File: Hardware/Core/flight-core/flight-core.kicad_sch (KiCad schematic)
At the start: 11 parts, among them J1 CONN_02x03_RA, J101 Conn_01x02, J106 Conn_01x02, J107 Conn_01x02, J2 CONN_02x03_RA, J3 CONN_02x03_RA, J4 CONN_02x03_RA, U2 DC DC CONVERTER 12V 240W

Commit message: adding logical gate structure without RC components in bus arbitration logic sch file
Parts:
- removed R2: R_100K, footprints:R_0805_OEM, symbol formula:R_100K
- added D1: LED_0805_Amber, footprints:LED_0805_OEM, symbol formula:LED_0805_Amber
- added J10, J12, J8, J9: Conn_02x05_Counter_Clockwise, Connector_Molex:Molex_Micro-Fit_3.0_43045-1000_2x05_P3.00mm_Horizontal, symbol Connector_Generic:Conn_02x05_Counter_Clockwise
- added J11, J13, J14, J15, J16, J17, J18, J19: Conn_01x02, Connector_Molex:Molex_Micro-Fit_3.0_43650-0200_1x02_P3.00mm_Horizontal, symbol Connector_Generic:Conn_01x02
- added J20: Conn_01x04, Connector_Molex:Molex_Micro-Fit_3.0_43650-0400_1x04_P3.00mm_Horizontal, symbol Connector_Generic:Conn_01x04
- added J5: Cube Orange Plus Female Header, DF17_4.0_-80DP-0.5V_57_:HRS_DF17_4.0_-80DP-0.5V_57_, symbol formula:DF17_4.0_-80DP-0.5V_57_
- added J7: Conn_01x02, symbol Connector_Generic:Conn_01x02
- added R2, R4: 120R, OEM:R_0603, symbol OEM:120R
- added R3: R_100K, footprints:R_0805_OEM, symbol formula:R_100K
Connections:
- net +5V: now also J20.1 (Pin_1), J5.61, J5.63
- net CAN+_END: now also R4.2
- net CAN+_N: now also R2.2
- net CAN-_END: now also R4.1
- net CAN-_N: now also R2.1
- net GND: now also D1.1 (K), J20.2 (Pin_2), J5.13, J5.15, J5.18, J5.40, R3.2
- net MATE_DETECT_E: now also J10.8 (Pin_8)
- net MATE_DETECT_N: now also J12.8 (Pin_8)
- net MATE_DETECT_S: now also J9.8 (Pin_8)
- net MATE_DETECT_W: now also J8.8 (Pin_8)
- net WIRELESS_ESTOP: now reaches J101.2 (Pin_2)
- net WIRELESS_ESTOP: now also J7.1 (Pin_1)
- new net: J7.2 (Pin_2), R3.1
- new net: D1.2 (A), J5.2
- new net CAN+: J5.79
- new net CAN-: J5.77
- new net CANBE+: J8.10 (Pin_10)
- new net CANBE-: J8.9 (Pin_9)
- new net CANBN+: J12.10 (Pin_10)
- new net CANBN-: J12.9 (Pin_9)
- new net CANBS+: J9.10 (Pin_10)
- new net CANBS-: J9.9 (Pin_9)
- new net CANBW+: J10.10 (Pin_10)
- new net CANBW-: J10.9 (Pin_9)
- new net CANME+: J17.1 (Pin_1)
- new net CANME-: J17.2 (Pin_2)
- new net CANMN+: J19.1 (Pin_1)
- new net CANMN-: J19.2 (Pin_2)
- new net CANMNE+: J18.1 (Pin_1)
- new net CANMNE-: J18.2 (Pin_2)
- new net CANMNW+: J11.1 (Pin_1)
- new net CANMNW-: J11.2 (Pin_2)
- new net CANMS+: J15.1 (Pin_1)
- new net CANMS-: J15.2 (Pin_2)
- new net CANMSE+: J16.1 (Pin_1)
- new net CANMSE-: J16.2 (Pin_2)
- new net CANMSW+: J14.1 (Pin_1)
- new net CANMSW-: J14.2 (Pin_2)
- new net CANMW+: J13.1 (Pin_1)
- new net CANMW-: J13.2 (Pin_2)
- new net CAN_GPS+: J20.3 (Pin_3)
- new net CAN_GPS-: J20.4 (Pin_4)
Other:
- removed sheet Cube connector
- added sheet CAN Repeater (can_repeater.kicad_sch)
- moved on the sheet: J1, J101, J2, J3, J4, R101, R102, U2

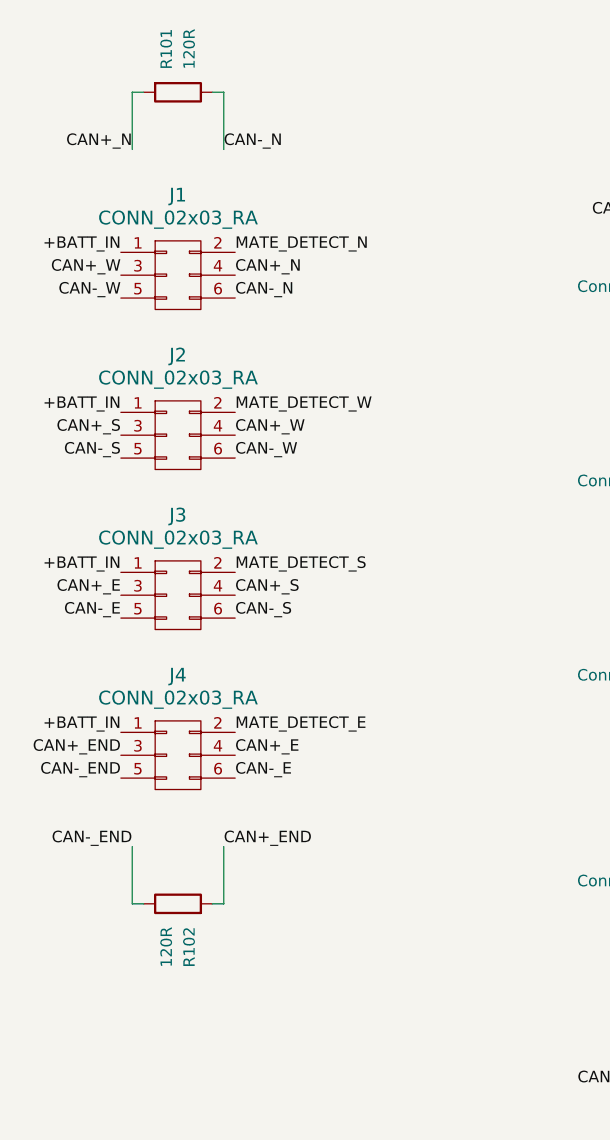
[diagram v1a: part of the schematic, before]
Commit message: moving multi-unit parts into OlinBAD library; added 0603 0.1uF cap
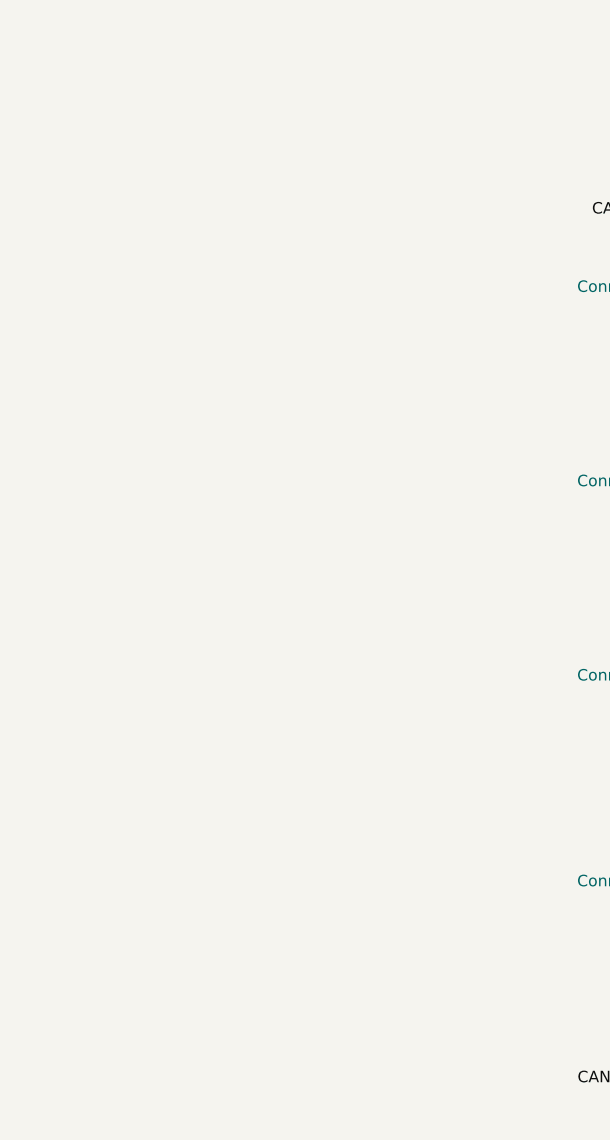
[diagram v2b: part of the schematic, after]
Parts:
- removed J1, J2, J4: CONN_02x03_RA, CONN06_1724480006_MOL, symbol formula:CONN_02x03_RA
- removed J3: CONN_02x03_RA, footprints:CONN06_1724480006_MOL, symbol formula:CONN_02x03_RA
- removed R101, R102: 120R, OEM:R_0603, symbol OEM:120R

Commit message: added many shutdown nodes, can_repeater instances, separated arm_connectors, basic stm32 peripherals
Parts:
- removed J106, J107: Conn_01x02, symbol Connector_Generic:Conn_01x02
- removed J11, J13, J14, J15, J16, J17, J18, J19: Conn_01x02, Connector_Molex:Molex_Micro-Fit_3.0_43650-0200_1x02_P3.00mm_Horizontal, symbol Connector_Generic:Conn_01x02
- removed U2: DC DC CONVERTER 12V 240W, symbol formula:DC_DC_CONVERTER_12V_240W
- added C13: C_10uF, footprints:C_0603_1608Metric, symbol Device:C
- added C2: 22uF, footprints:C_0603_1608Metric, symbol Device:C
- added J2: Conn_01x08, symbol Connector_Generic:Conn_01x08
- added J21, J22, J23, J24, J25, J26, J27, J28, J29, J3, J30, J4, J6: Conn_01x02, symbol Connector_Generic:Conn_01x02
- added L2: L_470nH, obad_footprints:IND_XFL4015_COC, symbol OlinBAD:XFL4015-471MEC
- added Q1: BSS308PE, footprints:SOT-23-3_OEM, symbol formula:BSS308PE
- added R10, R107, R11, R12, R14, R6, R7: 330, OEM:R_0603_1608Metric, symbol OEM:1KR
- added R13: R, symbol Device:R
- added R5: 1M, footprints:R_0603_1608Metric, symbol Device:R
- added U10, U103, U11, U13, U2, U3, U65: LTV-356T, Package_SO:SO-4_4.4x3.6mm_P2.54mm, symbol Isolator:LTV-356T
- added U12: 18-75V to 5V Converter, obad_footprints:UWE-Q12_MUR, symbol OlinBAD:E36SC05025NRFA
- added U4: TPS62086RLTR, obad_footprints:RLT0007A, symbol OlinBAD:TPS62086RLTR
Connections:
- net CAN+_N is gone; now on net CAN+: R2.2
- net CAN-_N is gone; now on net CAN-: R2.1
- net +3.3V: now also C2.1, L2.2, R5.1, U4.3 (FB), U4.4 (VOS)
- net +5V: now also C13.1, J2.1 (Pin_1), Q1.3 (D), R13.1, U12.8 (VOUT+), U4.1 (EN), U4.7 (VIN)
- net +BATT: now also J10.1 (Pin_1), J12.1 (Pin_1), J8.1 (Pin_1), J9.1 (Pin_1), U12.1 (VIN+)
- net GND: now also C13.2, C2.2, J2.2 (Pin_2), U10.2, U103.2, U11.2, U12.3 (VIN-), U12.4 (VOUT-), U13.2, U2.2, U3.2, U4.5 (GND), U65.2
- net at R3.1: now also J25.2 (Pin_2); no longer J7.2 (Pin_2)
- net ARM: now reaches J9.2 (Pin_2)
- net ARM: now also J10.2 (Pin_2), J12.2 (Pin_2), J8.2 (Pin_2)
- net BMS_OK_S: now reaches J9.6 (Pin_6)
- net BMS_OK_S: now also R11.1
- net SHDN_SENSE_BMS_MATE_S: now reaches J9.7 (Pin_7)
- net SHDN_SENSE_BMS_MATE_S: now also U3.4
- net BMS_OK_W: now reaches J10.6 (Pin_6)
- net BMS_OK_W: now also R12.1
- net SHDN_SENSE_BMS_MATE_W: now reaches J10.7 (Pin_7)
- net SHDN_SENSE_BMS_MATE_W: now also U11.4
- net BMS_OK_N: now reaches J12.6 (Pin_6)
- net BMS_OK_N: now also R107.1
- net SHDN_SENSE_BMS_MATE_N: now reaches J12.7 (Pin_7)
- net SHDN_SENSE_BMS_MATE_N: now also U103.4
- net BMS_OK_E: now reaches J8.6 (Pin_6)
- net BMS_OK_E: now also R10.1
- net SHDN_SENSE_BMS_MATE_E: now reaches J8.7 (Pin_7)
- net SHDN_SENSE_BMS_MATE_E: now also U2.4
- net MATE_DETECT_E renamed SHDN_TO_BMS_MATE_W
- net SHDN_TO_BMS_MATE_W: now also U3.3
- net MATE_DETECT_N renamed SHDN_TO_BMS_MATE_N
- net MATE_DETECT_S renamed SHDN_TO_BMS_MATE_S
- net SHDN_TO_BMS_MATE_S: now also U2.3
- net MATE_DETECT_W renamed SHDN_TO_BMS_MATE_E
- net SHDN_TO_BMS_MATE_E: now also U103.3
- net RIDER_ESTOP renamed SHDN_TO_REMOTE_ESTOP
- net WIRELESS_ESTOP renamed SHDN_SENSE_REMOTE_ESTOP
- net SHDN_SENSE_REMOTE_ESTOP: no longer J7.1 (Pin_1)
- new net: R11.2, U3.1
- new net: Q1.1 (G), R13.2
- new net: L2.1, U4.6 (SW)
- new net: R5.2, U4.2 (PG)
- new net: R7.2, U65.1
- new net: R14.1, U13.1
- new net: Q1.2 (S), R14.2
- new net: R12.2, U11.1
- new net: R6.2, U10.1
- new net: R107.2, U103.1
- new net: R10.2, U2.1
- new net ALL_BMS_OK: U11.3
- new net ALL_BMS_OK_MATED: J3.1 (Pin_1)
- new net CAN+_SENSE: J2.3 (Pin_3)
- new net CAN-_SENSE: J2.4 (Pin_4)
- new net CUBE_OK: R6.1
- new net GPIO_SENSE1: J2.5 (Pin_5)
- new net GPIO_SENSE2: J2.6 (Pin_6)
- new net GPIO_SENSE3: J2.7 (Pin_7)
- new net GPIO_SENSE4: J2.8 (Pin_8)
- new net SANITY_CHECK: R7.1
- new net SHDN_SENSE_CUBE: U10.3
- new net SHDN_SENSE_FRAME_ESTOP: J27.2 (Pin_2)
- new net SHDN_SENSE_NUC: J30.2 (Pin_2)
- new net SHDN_SENSE_RIDER_ESTOP: J28.2 (Pin_2)
- new net SHDN_SENSE_STM: U65.3
- new net SHDN_SENSE_TILT: J29.2 (Pin_2)
- new net SHDN_SENSE_TSMS: J26.2 (Pin_2)
- new net SHDN_SENSE_WIRED_ESTOP: J7.2 (Pin_2)
- new net SHDN_TO_CUBE: U10.4
- new net SHDN_TO_FRAME_ESTOP: J27.1 (Pin_1)
- new net SHDN_TO_NE_ARM: J3.2 (Pin_2), J4.1 (Pin_1)
- new net SHDN_TO_NUC: J30.1 (Pin_1)
- new net SHDN_TO_RIDER_ESTOP: J28.1 (Pin_1)
- new net SHDN_TO_STM: U65.4
- new net SHDN_TO_TILT: J29.1 (Pin_1)
- new net SHDN_TO_TSMS: J26.1 (Pin_1)
- new net SHDN_TO_WIRED_ESTOP: J7.1 (Pin_1)
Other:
- removed sheet CAN Repeater
- added sheet Arm Connectors (arm_connectors.kicad_sch)
- added sheet CAN Repeater10 (can_repeater.kicad_sch)
- added sheet CAN Repeater11 (can_repeater.kicad_sch)
- added sheet CAN Repeater12 (can_repeater.kicad_sch)
- added sheet CAN Repeater13 (can_repeater.kicad_sch)
- added sheet CAN Repeater14 (can_repeater.kicad_sch)
- added sheet CAN Repeater9 (can_repeater.kicad_sch)
- sheet stm32 ports: added +3.3V, +5V, CAN+, CAN-, GPIO_SENSE1, GPIO_SENSE2, GPIO_SENSE3, GPIO_SENSE4; removed none
- moved on the sheet: D1, J10, J101, J12, J20, J5, J7, J8, J9, R2, R3, R4

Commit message: renaming the values of LRC generics to just the value with unit letter (except resistors are just the value)
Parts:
- removed L2: L_470nH, obad_footprints:IND_XFL4015_COC, symbol OlinBAD:XFL4015-471MEC
- removed Q1: BSS308PE, footprints:SOT-23-3_OEM, symbol formula:BSS308PE
- removed R13: R, symbol Device:R
- removed R14: 330, OEM:R_0603_1608Metric, symbol OEM:1KR
- removed U13: LTV-356T, Package_SO:SO-4_4.4x3.6mm_P2.54mm, symbol Isolator:LTV-356T
- added L1: 470nH, obad_footprints:IND_XFL4015_COC, symbol OlinBAD:XFL4015-471MEC
- C13: value C_10uF -> 10uF
- R2, R4: value 120R -> 120
- R3: value R_100K -> 100K
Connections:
- net ALL_BMS_OK_MATED is gone; now on net SHDN_SENSE_ALL_BATT: J3.1 (Pin_1)
- net SHDN_TO_BMS_MATE_N is gone; now on net SHDN_SENSE_NUC: J12.8 (Pin_8)
- net SHDN_TO_CUBE is gone; now on net SHDN_SENSE_TILT: U10.4
- net SHDN_TO_FRAME_ESTOP is gone; now on net SHDN_SENSE_TSMS: J27.1 (Pin_1)
- net SHDN_TO_NUC is gone; now on net SHDN_SENSE_STM: J30.1 (Pin_1)
- net SHDN_TO_REMOTE_ESTOP is gone; now on net SHDN_SENSE_RIDER_ESTOP: J101.1 (Pin_1)
- net SHDN_TO_RIDER_ESTOP is gone; now on net SHDN_SENSE_FRAME_ESTOP: J28.1 (Pin_1)
- net SHDN_TO_STM is gone; now on net SHDN_SENSE_CRITICAL: U65.4
- net SHDN_TO_TILT is gone; now on net SHDN_SENSE_WIRED_ESTOP: J29.1 (Pin_1)
- net SHDN_TO_TSMS is gone; now on net +5V: J26.1 (Pin_1)
- net SHDN_TO_WIRED_ESTOP is gone; now on net SHDN_SENSE_REMOTE_ESTOP: J7.1 (Pin_1)
- net +3.3V: now also L1.2
- net SHDN_SENSE_SW_ARM: now reaches J24.1 (Pin_1)
- net SHDN_SENSE_SW_ARM: now also J23.2 (Pin_2)
- net SHDN_SENSE_W_ARM: now reaches J24.2 (Pin_2)
- net SHDN_SENSE_W_ARM: now also J25.1 (Pin_1)
- net at U4.6 (SW): now also L1.1
- net SHDN_SENSE_S_ARM: now reaches J23.1 (Pin_1)
- net SHDN_SENSE_S_ARM: now also J22.2 (Pin_2)
- net SHDN_SENSE_NW_ARM: now reaches J25.2 (Pin_2), R3.1
- net SHDN_SENSE_SE_ARM: now reaches J22.1 (Pin_1)
- net SHDN_SENSE_SE_ARM: now also J21.2 (Pin_2)
- net SHDN_SENSE_NE_ARM: now reaches J6.1 (Pin_1)
- net SHDN_SENSE_NE_ARM: now also J4.2 (Pin_2)
- net SHDN_SENSE_E_ARM: now reaches J6.2 (Pin_2)
- net SHDN_SENSE_E_ARM: now also J21.1 (Pin_1)
- net ALL_BMS_OK renamed SHDN_SENSE_ALL_BATT
- net SHDN_SENSE_CUBE renamed SHDN_SENSE_CRITICAL
- net SHDN_TO_BMS_MATE_E renamed SHDN_SENSE_BMS_OK_N
- net SHDN_TO_BMS_MATE_S renamed SHDN_SENSE_BMS_OK_E
- net SHDN_TO_BMS_MATE_W renamed SHDN_SENSE_BMS_OK_S
- net SHDN_TO_NE_ARM renamed SHDN_SENSE_N_ARM
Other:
- moved on the sheet: J101, J21, J22, J23, J24, J25, J26, J27, J28, J29, J3, J30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

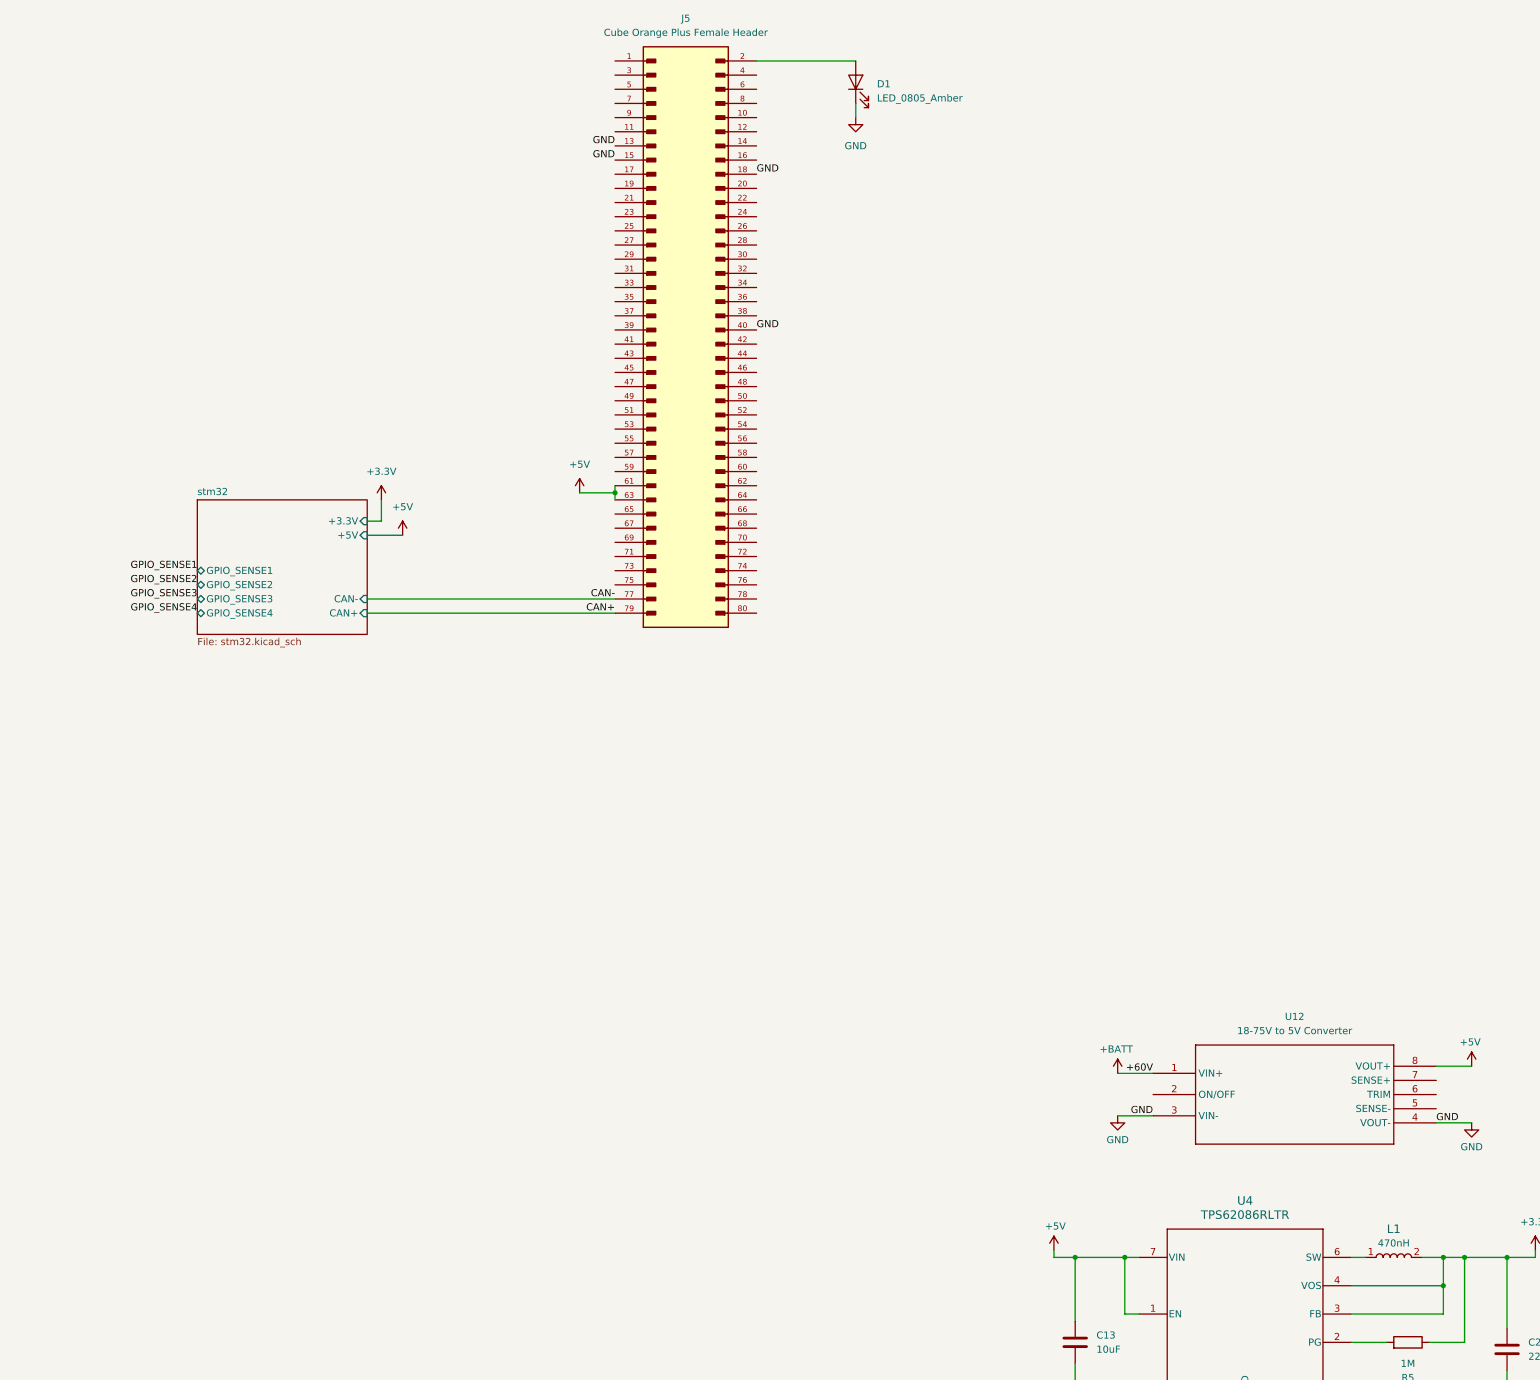
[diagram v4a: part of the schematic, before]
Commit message: adding full chain of shutdown nodes
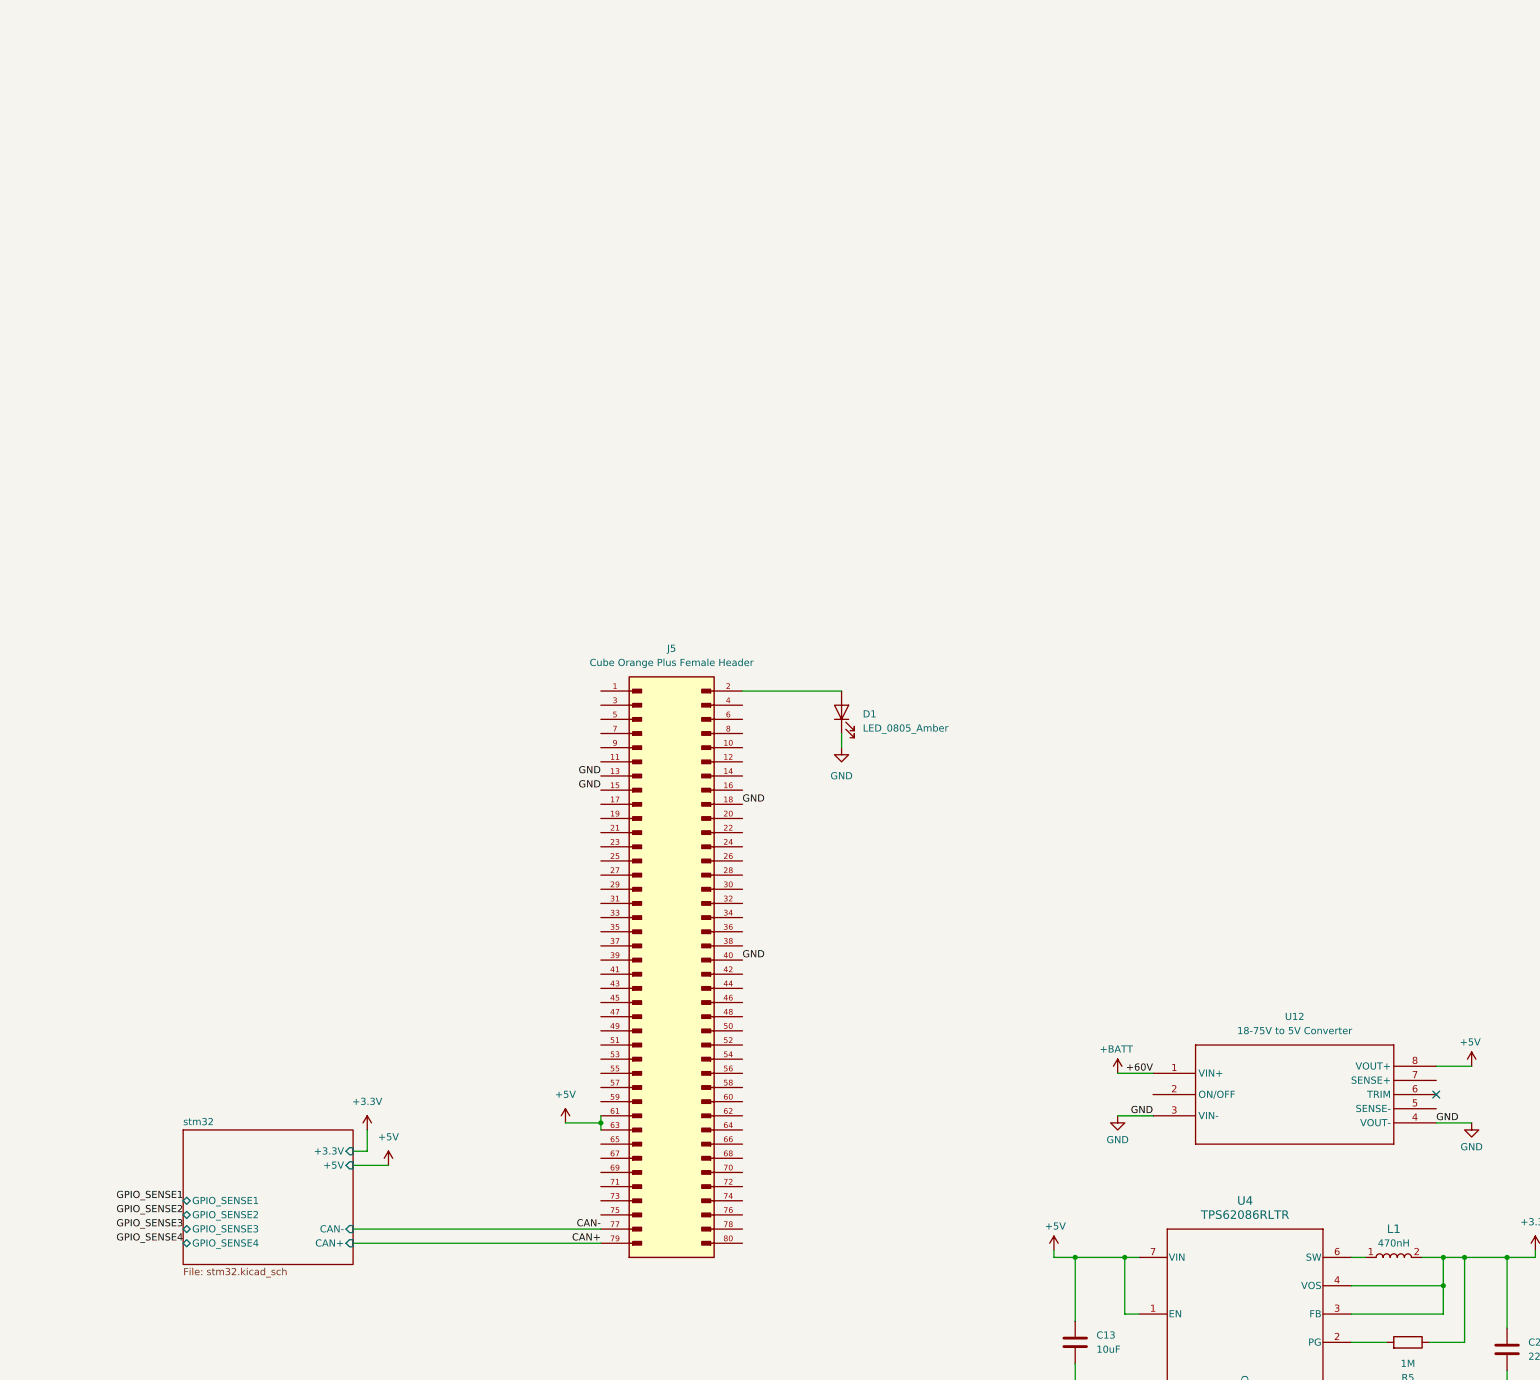
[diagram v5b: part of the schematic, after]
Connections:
- no-connect marks 0 -> 1
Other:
- moved on the sheet: D1, J5
